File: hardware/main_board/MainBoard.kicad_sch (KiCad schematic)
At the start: 56 parts, among them J1 5V In, J2 9V In, J3 Conn_01x08, J4 Conn_01x08, J5 Conn_01x08, J6 Conn_01x08, U1 TPIC6595, U2 ESP32-C6, U3 SD_Breakout, U4 TPIC6595, U5 TPIC6595, U6 TPIC6595

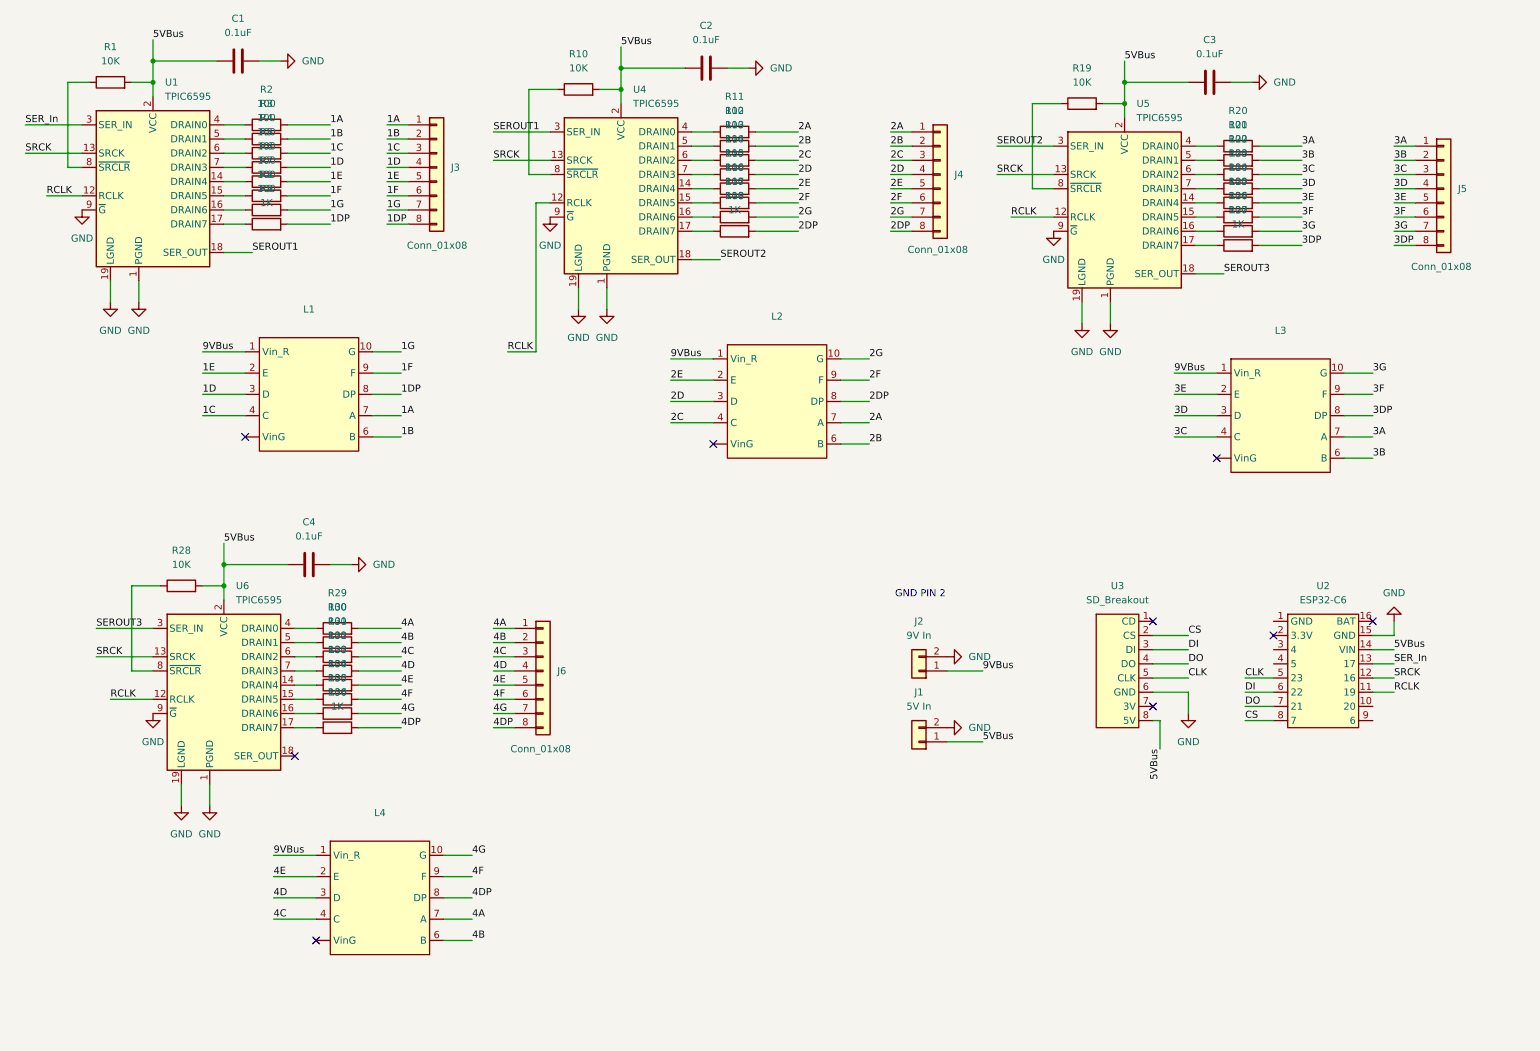
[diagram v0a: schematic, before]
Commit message: Updated main_boad sch | Created btn_board files
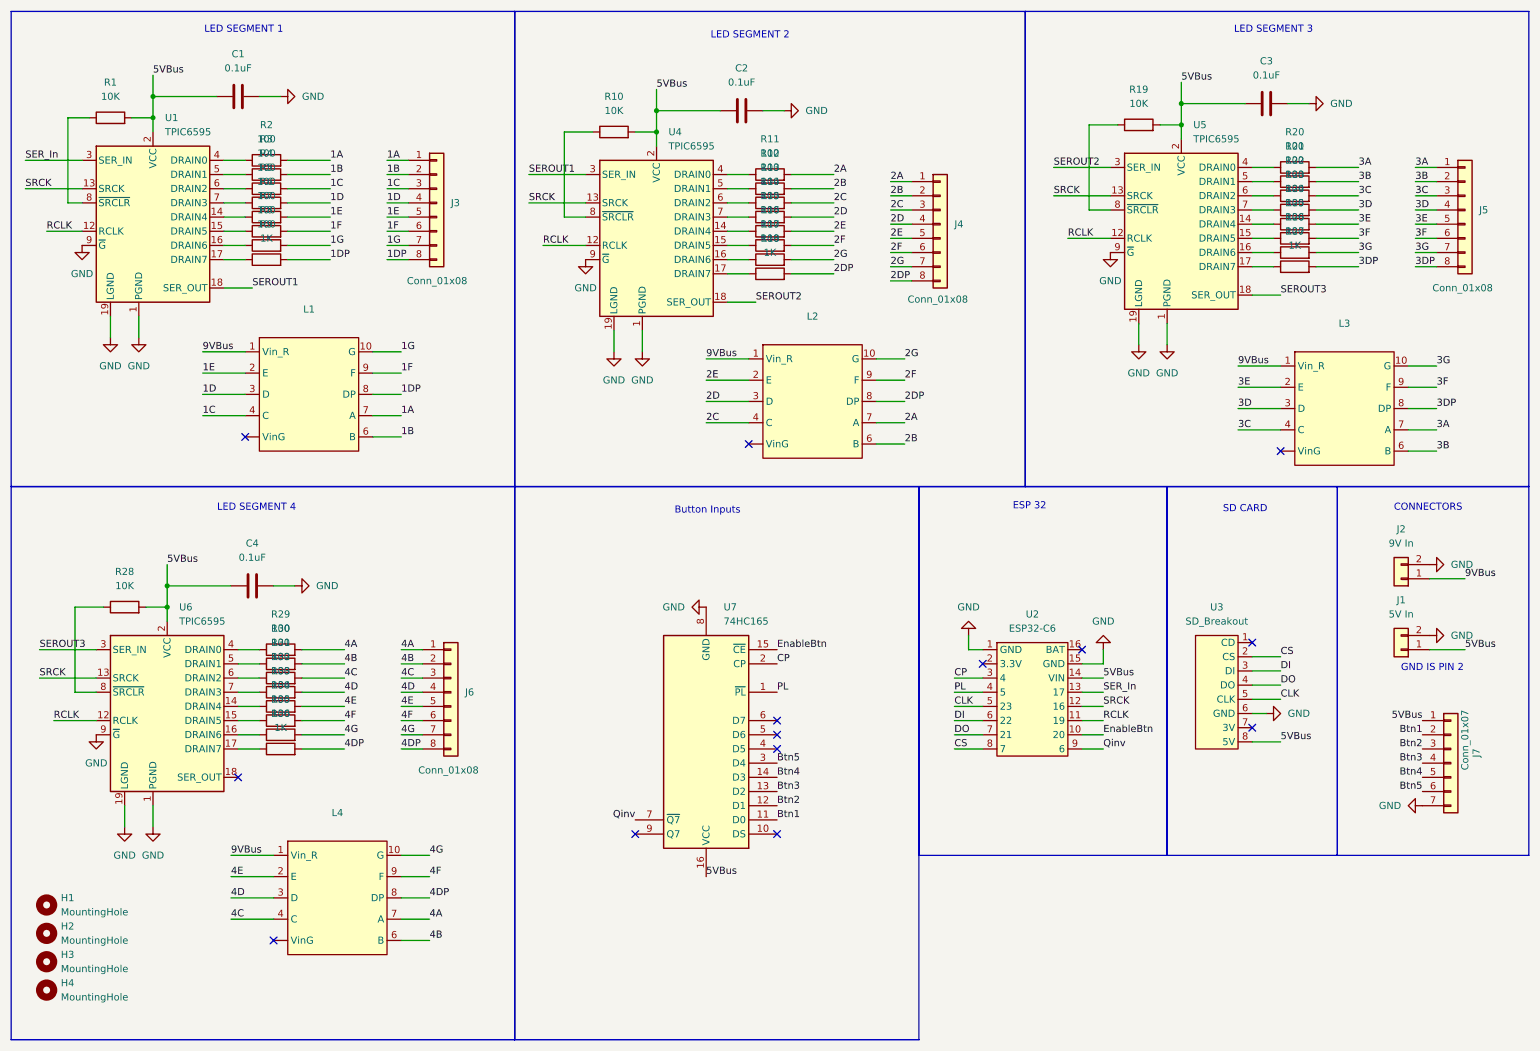
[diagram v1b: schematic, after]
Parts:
- added H1, H2, H3, H4: MountingHole, symbol Mechanical:MountingHole
- added J7: Conn_01x07, symbol Connector_Generic:Conn_01x07
- added U7: 74HC165, Package_DIP:DIP-16_W7.62mm_Socket, symbol 74xx:74HC165
- C1, C2, C3, C4: footprint (none) -> Capacitor_SMD:C_1206_3216Metric_Pad1.33x1.80mm_HandSolder
- J3, J4, J5, J6: footprint (none) -> Connector_PinHeader_2.54mm:PinHeader_1x08_P2.54mm_Vertical
- R1, R10, R11, R12, R13, R14, R15, R16, R17, R18, R19, R2, R20, R21, R22, R23, R24, R25, R26, R27, R28, R29, R3, R30, R31, R32, R33, R34, R35, R36, R4, R5, R6, R7, R8, R9: footprint (none) -> Resistor_SMD:R_1206_3216Metric_Pad1.30x1.75mm_HandSolder
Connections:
- net 5VBus: now also J7.1 (Pin_1), U7.16 (VCC)
- net GND: now also U2.1 (GND), J7.7 (Pin_7), U7.8 (GND)
- net EnableBtn: now reaches U2.10 (20)
- net EnableBtn: now also U7.15 (~{CE})
- net CP: now reaches U2.3 (4)
- net CP: now also U7.2 (CP)
- net PL: now reaches U2.4 (5)
- net PL: now also U7.1 (~{PL})
- net Qinv: now reaches U2.9 (6)
- net Qinv: now also U7.7 (~{Q7})
- new net Btn1: J7.2 (Pin_2), U7.11 (D0)
- new net Btn2: J7.3 (Pin_3), U7.12 (D1)
- new net Btn3: J7.4 (Pin_4), U7.13 (D2)
- new net Btn4: J7.5 (Pin_5), U7.14 (D3)
- new net Btn5: J7.6 (Pin_6), U7.3 (D4)
- no-connect marks 9 -> 14
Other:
- note added: "Button Inputs"
- note added: "CONNECTORS"
- note added: "ESP 32"
- note added: "GND IS PIN 2"
- note added: "LED SEGMENT 1"
- note added: "LED SEGMENT 2"
- note added: "LED SEGMENT 3"
- note added: "LED SEGMENT 4"
- note added: "SD CARD"
- note removed: "GND PIN 2"
- moved on the sheet: C1, C2, C3, C4, J1, J2, J3, J4, J5, J6, L2, L3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

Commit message: Updated main board to finish footprint assignment
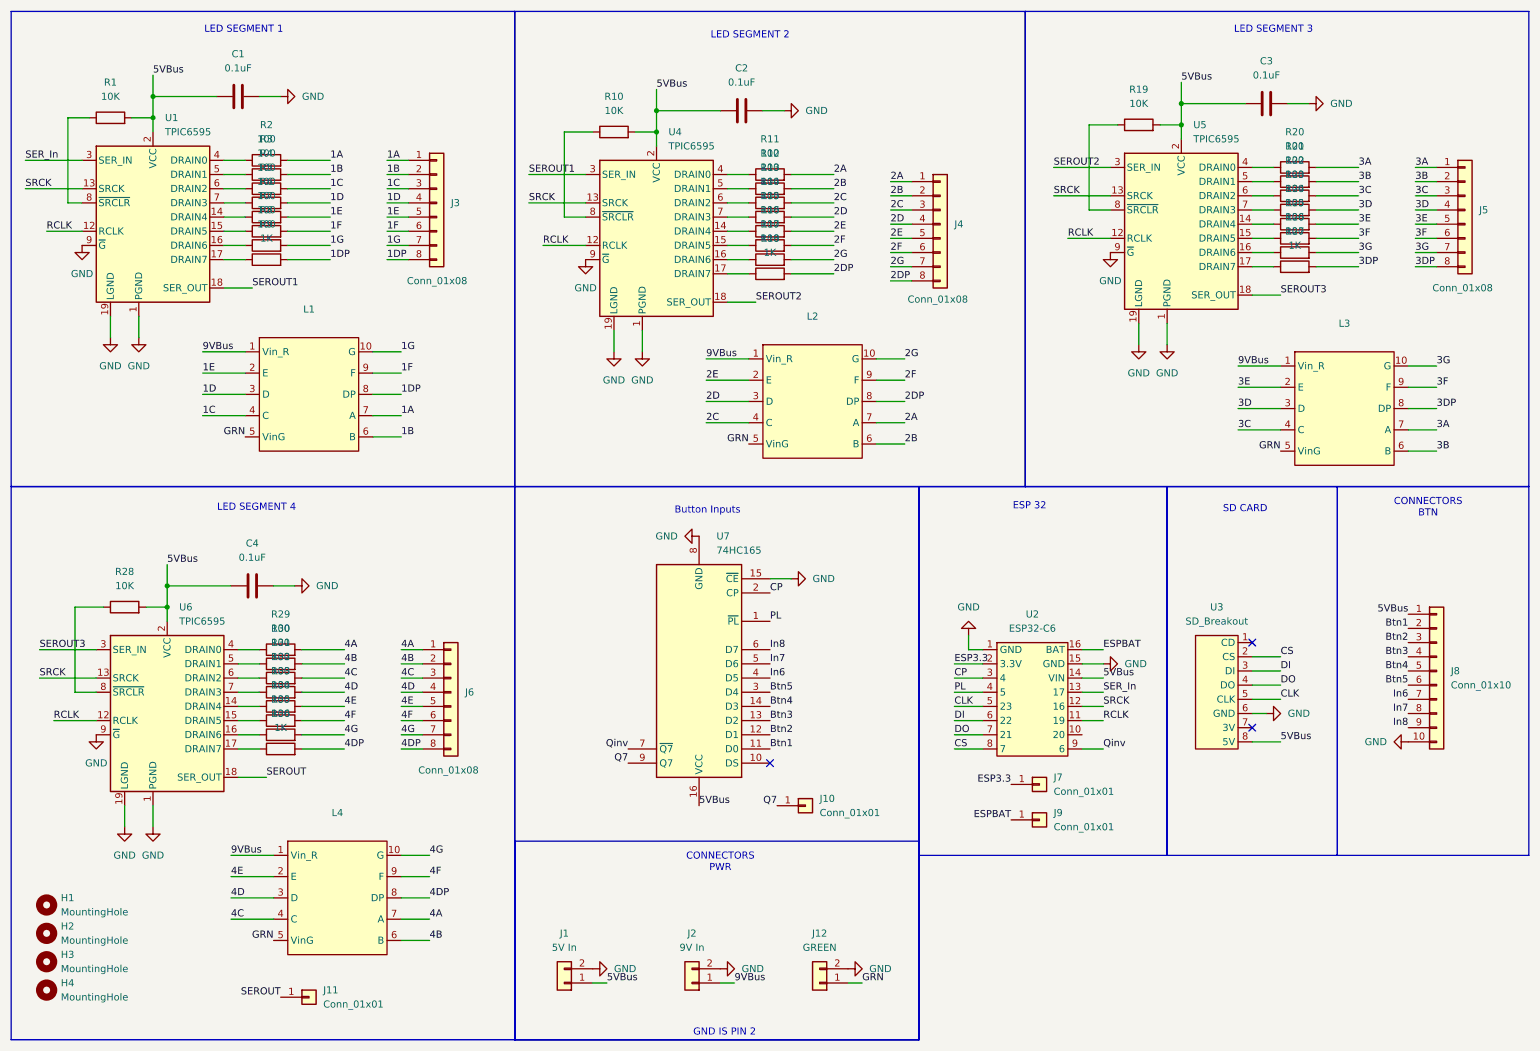
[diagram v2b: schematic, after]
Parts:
- removed J7: Conn_01x07, symbol Connector_Generic:Conn_01x07
- added J10, J11, J7, J9: Conn_01x01, Connector_PinSocket_2.54mm:PinSocket_1x01_P2.54mm_Vertical, symbol Connector_Generic:Conn_01x01
- added J12: GREEN, Connector_JST:JST_EH_B2B-EH-A_1x02_P2.50mm_Vertical, symbol Connector_Generic:Conn_01x02
- added J8: Conn_01x10, GregFootprints:MOLEX_10_PIN, symbol Connector_Generic:Conn_01x10
- H1, H2, H3, H4: footprint (none) -> MountingHole:MountingHole_3.2mm_M3
- L1, L2, L3, L4: footprint (none) -> GregFootprints:7SEG_LED_2.3IN
- U2: footprint (none) -> GregFootprints:ESPC6_BEETLE
- U3: footprint (none) -> Connector_PinHeader_2.54mm:PinHeader_1x08_P2.54mm_Vertical
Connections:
- net 5VBus: now also J8.1 (Pin_1)
- net Btn1: now also J8.2 (Pin_2)
- net Btn2: now also J8.3 (Pin_3)
- net Btn3: now also J8.4 (Pin_4)
- net Btn4: now also J8.5 (Pin_5)
- net Btn5: now also J8.6 (Pin_6)
- net GND: now also U7.15 (~{CE}), J12.2 (Pin_2), J8.10 (Pin_10)
- net ESPBAT: now reaches U2.16 (BAT)
- net ESPBAT: now also J9.1 (Pin_1)
- net ESP3.3: now reaches U2.2 (3.3V)
- net ESP3.3: now also J7.1 (Pin_1)
- net SEROUT: now reaches U6.18 (SER_OUT)
- net SEROUT: now also J11.1 (Pin_1)
- net In6: now reaches U7.4 (D5)
- net In6: now also J8.7 (Pin_7)
- net In7: now reaches U7.5 (D6)
- net In7: now also J8.8 (Pin_8)
- net In8: now reaches U7.6 (D7)
- net In8: now also J8.9 (Pin_9)
- net Q7: now reaches U7.9 (Q7)
- net Q7: now also J10.1 (Pin_1)
- net EnableBtn: no longer names the net of U2.10 (20)
- net EnableBtn: no longer U7.15 (~{CE})
- new net GRN: J12.1 (Pin_1), L1.5 (VinG), L2.5 (VinG), L3.5 (VinG), L4.5 (VinG)
- no-connect marks 14 -> 3
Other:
- note added: "CONNECTORS BTN"
- note added: "CONNECTORS PWR"
- note removed: "CONNECTORS"
- moved on the sheet: J1, J2, U7

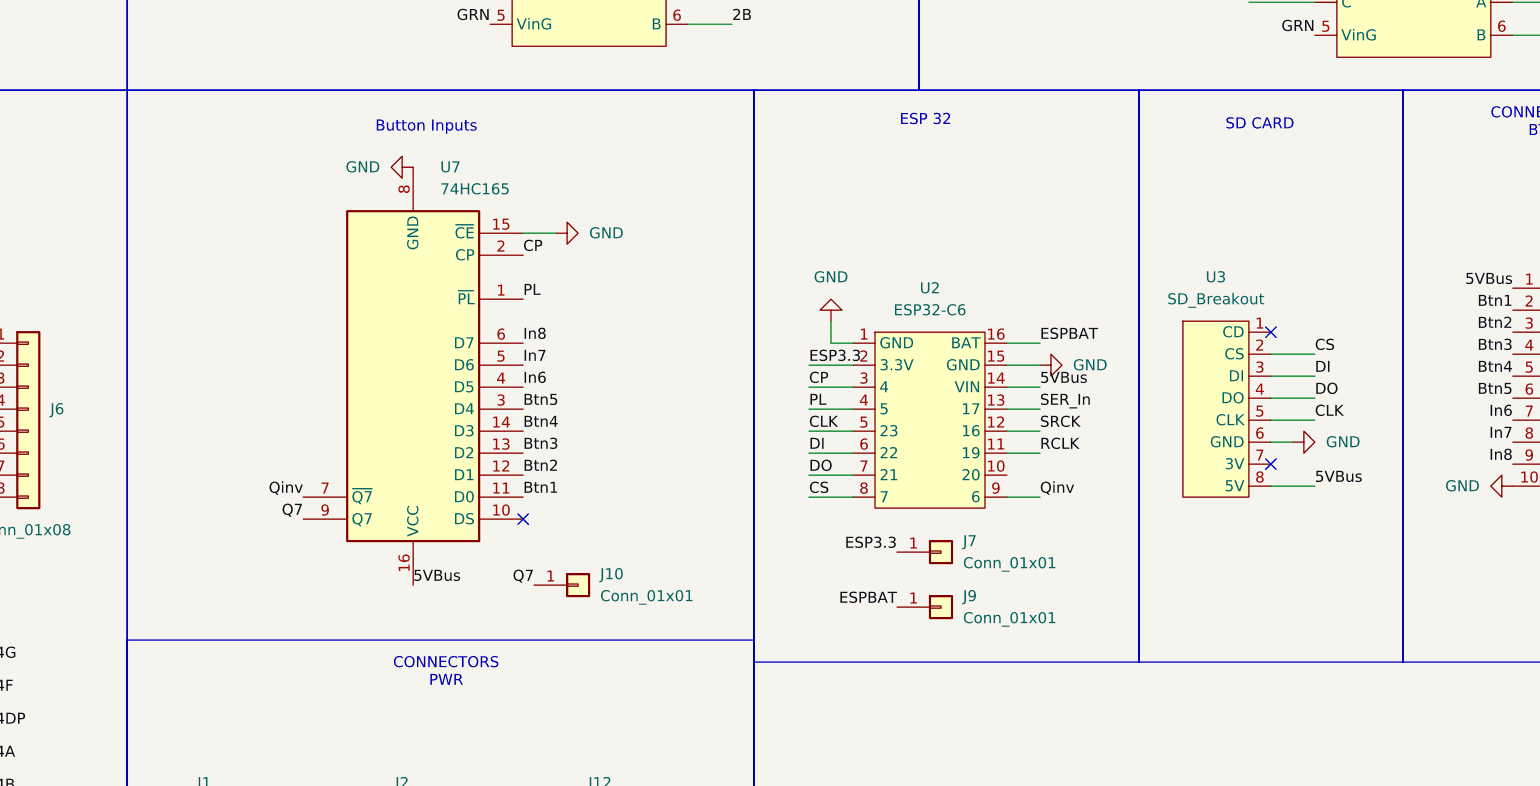
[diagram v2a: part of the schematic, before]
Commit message: Started PCB layout for mainboard
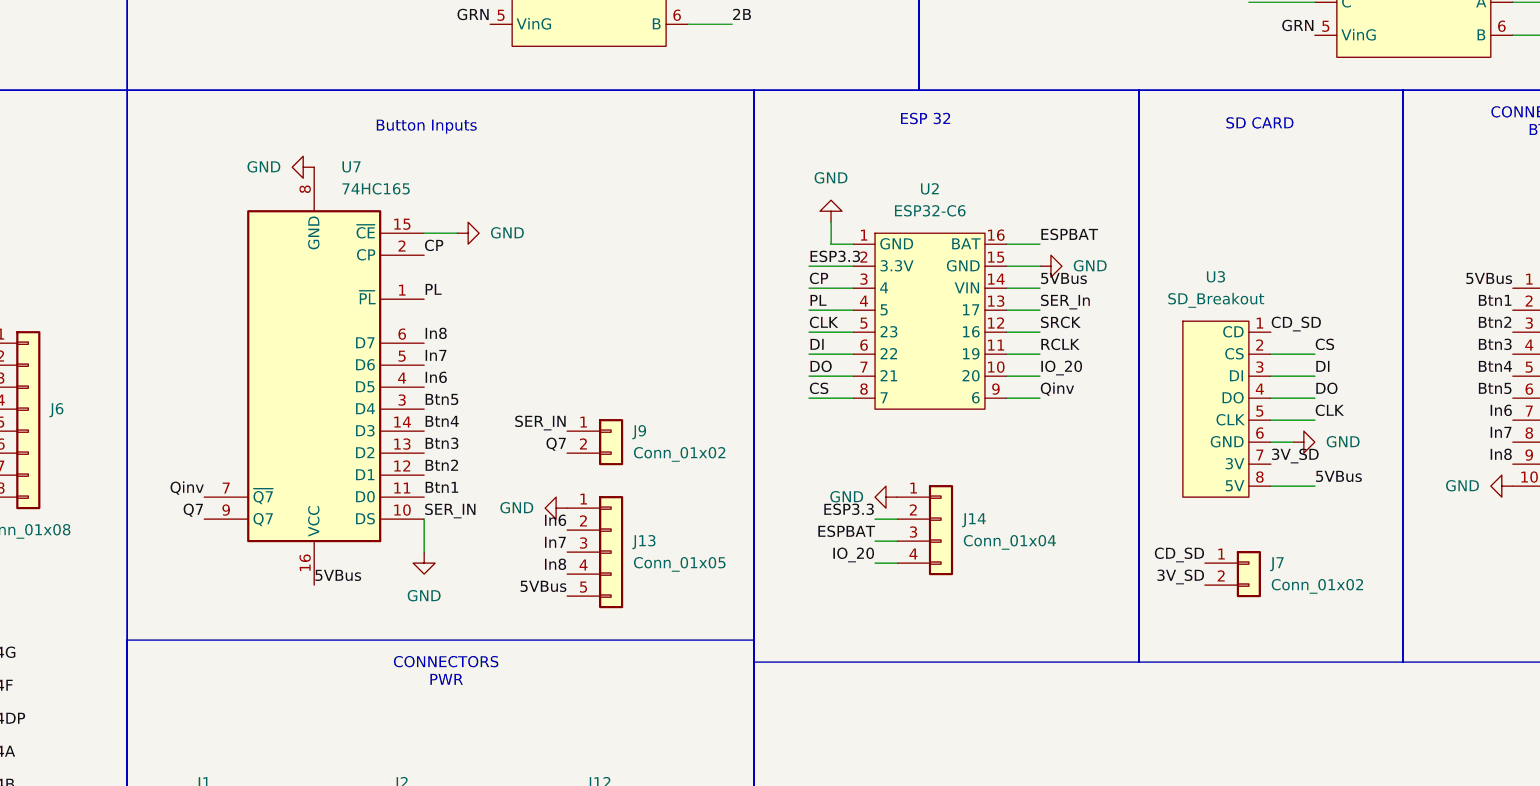
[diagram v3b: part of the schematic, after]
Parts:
- removed J10, J7, J9: Conn_01x01, Connector_PinSocket_2.54mm:PinSocket_1x01_P2.54mm_Vertical, symbol Connector_Generic:Conn_01x01
- added J13: Conn_01x05, Connector_PinHeader_2.54mm:PinHeader_1x05_P2.54mm_Vertical, symbol Connector_Generic:Conn_01x05
- added J14: Conn_01x04, Connector_PinHeader_2.54mm:PinHeader_1x04_P2.54mm_Vertical, symbol Connector_Generic:Conn_01x04
- added J7, J9: Conn_01x02, Connector_PinHeader_2.54mm:PinHeader_1x02_P2.54mm_Vertical, symbol Connector_Generic:Conn_01x02
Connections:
- net 5VBus: now also J13.5 (Pin_5)
- net ESP3.3: now also J14.2 (Pin_2)
- net ESPBAT: now also J14.3 (Pin_3)
- net GND: now also U7.10 (DS), J13.1 (Pin_1), J14.1 (Pin_1), J9.1 (Pin_1)
- net In6: now also J13.2 (Pin_2)
- net In7: now also J13.3 (Pin_3)
- net In8: now also J13.4 (Pin_4)
- net Q7: now also J9.2 (Pin_2)
- net IO_20: now reaches U2.10 (20)
- net IO_20: now also J14.4 (Pin_4)
- net CD_SD: now reaches U3.1 (CD)
- net CD_SD: now also J7.1 (Pin_1)
- net 3V_SD: now reaches U3.7 (3V)
- net 3V_SD: now also J7.2 (Pin_2)
- no-connect marks 3 -> 0
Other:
- moved on the sheet: U2, U7
